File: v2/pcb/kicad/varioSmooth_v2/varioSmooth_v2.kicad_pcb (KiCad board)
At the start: 2 copper layers, 33 parts, among them J1 USB_C_Receptacle_USB2.0_16P, SW1 SW_Push, U1 USBLC6-2SC6, U2 LTC4071xMS8E, U3 MDBT50Q-1MV2, U4 MS5611-01BA, Y1 32.768kHz

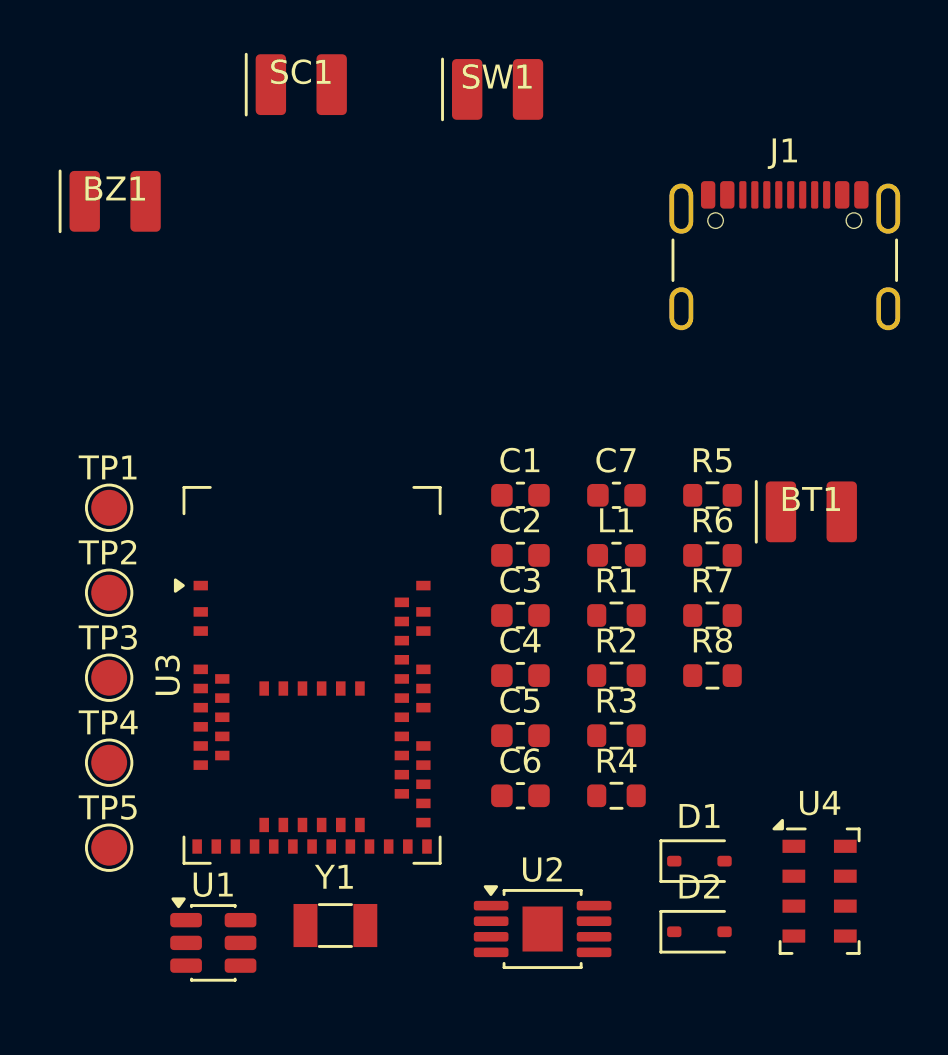
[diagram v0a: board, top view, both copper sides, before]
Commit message: Place and route the v2 helmet vario PCB
  Two-layer 20 x 32.75 mm board, single-sided assembly. The MDBT50Q antenna
  sits flush with the top edge and the USB-C receptacle at the bottom.
  Wire pads (solar cells, battery, buzzer, button) and the SWD/RESET/3V3/GND
  test pads are on the back.

  Routing was done by hand: the 32 kHz crystal next to the module, the
  VDDH/DCCH/L1 loop under it, USB D+/D- through the USBLC6 flow-through
  pads, then power, I2C, buzzer and SWD. GND pours cover both layers with
  stitching vias. The remaining DRC errors come from the USB-C footprint
  itself (hole clearance, starved thermals on A1/B12).

  Board rules: 0.15 mm minimum track, 0.3 mm edge clearance, 0.2 mm hole
  clearance.

  Add LCSC part numbers for JLCPCB assembly; U2 (LTC4071) stays
  hand-soldered.

  This USB version is kept as the development prototype; the compact
  helmet board without USB comes next.
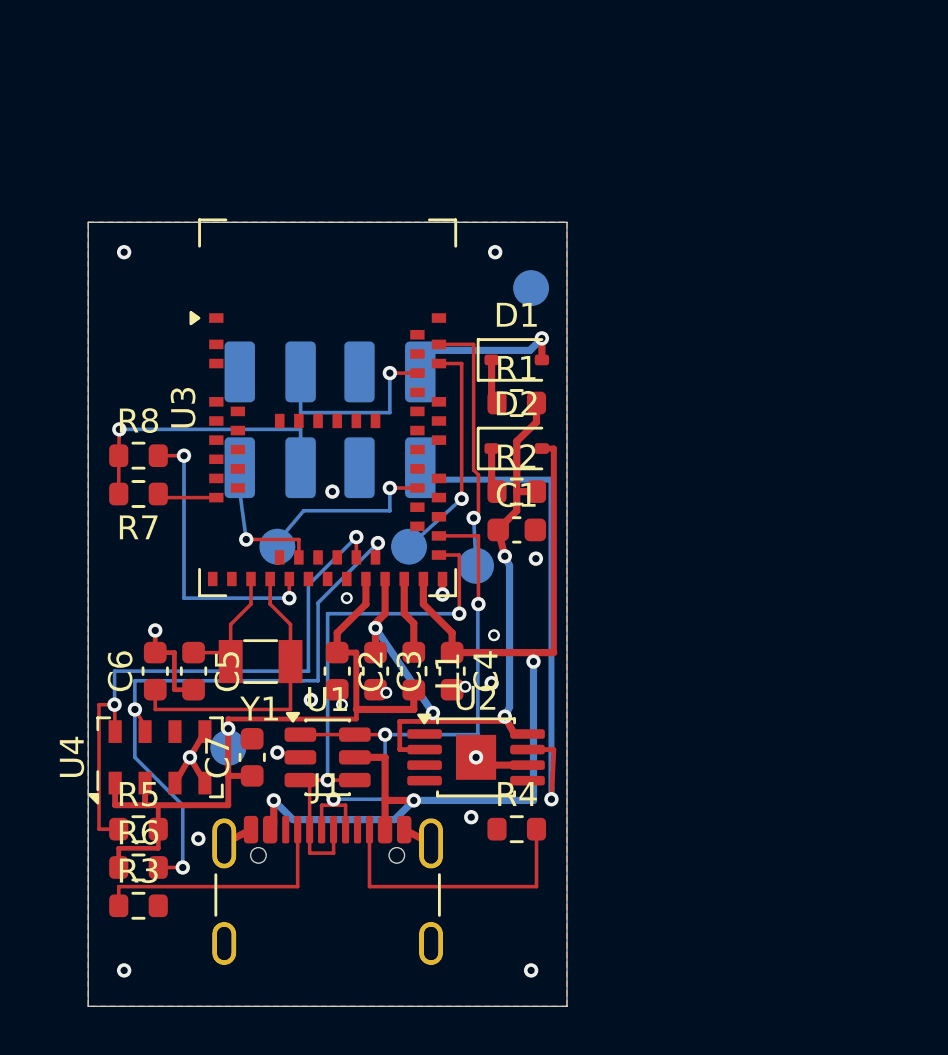
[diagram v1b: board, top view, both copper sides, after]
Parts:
- BT1, BZ1, SC1, SW1, TP1, TP2, TP3, TP4, TP5: moved to B.Cu
- moved J1 32.7 mm to (30.0, 51.3)
- moved TP5 29.3 mm to (38.5, 25.0), turned to 180 degrees
- moved U4 28.1 mm to (23.0, 44.6), turned to 90 degrees
- moved R5 27.7 mm to (22.1, 47.6)
- moved R6 27.3 mm to (22.1, 49.2)
- moved R8 25.7 mm to (22.1, 32.0)
- moved R7 24.5 mm to (22.1, 33.6), turned to 180 degrees
- moved D1 22.3 mm to (37.9, 28.0)
- moved D2 21.6 mm to (37.9, 31.7)
- moved R3 21.2 mm to (22.1, 50.8)
- moved C7 18.7 mm to (26.9, 44.6), turned to 90 degrees
- moved BT1 17.7 mm to (32.6, 32.5), turned to 180 degrees
- moved C6 16.1 mm to (22.8, 41.0), turned to 90 degrees
- moved TP2 15.4 mm to (36.2, 36.6), turned to 180 degrees
- moved SW1 15.1 mm to (27.6, 28.5), turned to 180 degrees
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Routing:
- net VBUS: track 0.00 -> 41.0 mm, vias 0 -> 3
- net +3.3V: track 0.00 -> 31.1 mm, vias 0 -> 1
- net VCC: track 0.00 -> 29.0 mm, vias 0 -> 4
- net /USB_D+: track 0.00 -> 25.5 mm, vias 0 -> 3
- net /I2C_SDA: track 0.00 -> 25.5 mm, vias 0 -> 3
- net /I2C_SCL: track 0.00 -> 24.6 mm, vias 0 -> 2
- net /USB_D-: track 0.00 -> 23.1 mm, vias 0 -> 2
- net Net-(BT1-+): track 0.00 -> 22.0 mm, vias 0 -> 1
- net /XL2: track 0.00 -> 12.3 mm
- net /BUZZ_A: track 0.00 -> 12.2 mm, vias 0 -> 2
- net GND: track 0.00 -> 11.8 mm, vias 0 -> 20
- net Net-(J1-CC2): track 0.00 -> 11.8 mm
- net Net-(BZ1-+): track 0.00 -> 11.0 mm, vias 0 -> 1
- net /SWDCLK: track 0.00 -> 10.9 mm, vias 0 -> 1
- net Net-(J1-CC1): track 0.00 -> 10.7 mm
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- added copper zone on B.Cu, net GND
- added copper zone on F.Cu, net GND
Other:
- board outline added: 20 x 32.8 mm
